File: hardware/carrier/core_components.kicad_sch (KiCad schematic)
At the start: 52 parts, among them J1 PANEL, J2 CARDKB, J3 HAPTIC, J4 EXT_LED, J5 PIEZ, J8 FRONTLIGHT, M1 Walter, Q1 UMH3N, Q2 SI1308EDL, Q3 MMST3904, SW1 KMR221GLFS, U1 CP2102N-A02-GQFN24, U2 SN74LVC2G126DCUR, U3 DRV2605LDGSR, U4 LIS2DW12TR

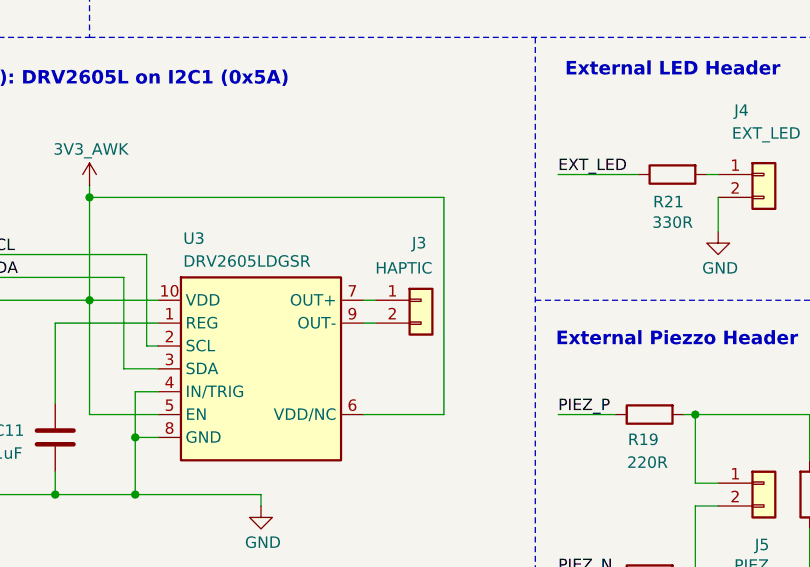
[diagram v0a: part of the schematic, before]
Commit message: Hand routed the carrier board
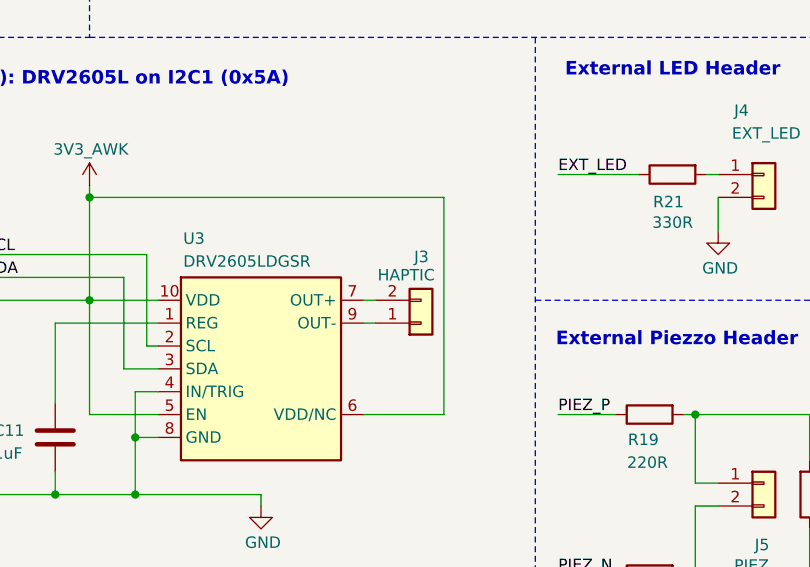
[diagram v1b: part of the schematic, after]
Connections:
- net at J3.1 (Pin_1): now also U3.9 (OUT-); no longer U3.7 (OUT+)
- net at J3.2 (Pin_2): now also U3.7 (OUT+); no longer U3.9 (OUT-)
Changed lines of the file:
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@@
 	(wire
 		(pts
+			(xy 351.79 162.56) (xy 353.06 162.56)
+		)
+		(stroke
+			(width 0)
+			(type default)
+		)
+	)
+	(wire
+		(pts
 			(xy 184.15 243.84) (xy 195.58 243.84)
 		)
@@
 	(wire
 		(pts
-			(xy 351.79 160.02) (xy 353.06 160.02)
-		)
-		(stroke
-			(width 0)
-			(type default)
-		)
-	)
-	(wire
-		(pts
 			(xy 87.63 198.12) (xy 92.71 198.12)
 		)
@@
 	(wire
 		(pts
-			(xy 351.79 162.56) (xy 353.06 162.56)
+			(xy 255.27 203.2) (xy 255.27 207.01)
 		)
 		(stroke
@@
 	(wire
 		(pts
-			(xy 255.27 203.2) (xy 255.27 207.01)
+			(xy 25.4 240.03) (xy 25.4 236.22)
 		)
 		(stroke
@@
 	(wire
 		(pts
-			(xy 25.4 240.03) (xy 25.4 236.22)
+			(xy 401.32 172.72) (xy 388.62 172.72)
 		)
 		(stroke
@@
 	(wire
 		(pts
-			(xy 401.32 172.72) (xy 388.62 172.72)
+			(xy 351.79 160.02) (xy 353.06 160.02)
 		)
 		(stroke
@@
 	(symbol
 		(lib_id "Connector_Generic:Conn_01x02")
-		(at 358.14 160.02 0)
+		(at 358.14 162.56 0)
+		(mirror x)
 		(unit 1)
 		(body_style 1)
@@
 		(dnp no)
 		(property "Reference" "J3"
-			(at 357.124 153.67 0)
+			(at 357.378 155.194 0)
 			(show_name no)
 			(do_not_autoplace no)
@@
 		)
 		(property "Value" "HAPTIC"
-			(at 353.06 156.464 0)
+			(at 359.664 157.226 0)
 			(show_name no)
 			(do_not_autoplace no)
@@
 					(size 1.27 1.27)
 				)
-				(justify left)
+				(justify right)
 			)
 		)
 		(property "Footprint" "Connector_JST:JST_SH_SM02B-SRSS-TB_1x02-1MP_P1.00mm_Horizontal"
-			(at 354.33 163.83 0)
+			(at 354.33 158.75 0)
 			(hide yes)
 			(show_name no)
@@
 		)
 		(property "Datasheet" "~"
-			(at 354.33 166.37 0)
+			(at 354.33 156.21 0)
 			(hide yes)
 			(show_name no)
@@
 		)
 		(property "Description" "Generic connector, single row, 01x02, script generated (kicad-library-utils/schlib/autogen/connector/)"
-			(at 354.33 168.91 0)
+			(at 354.33 153.67 0)
 			(hide yes)
 			(show_name no)
@@
 		)
 		(property "MPN" "SM02B-SRSS-TB"
-			(at 358.14 175.26 0)
+			(at 358.14 147.32 0)
 			(hide yes)
 			(show_name no)
@@
 		)
 		(property "LCSC" "C160402"
-			(at 358.14 177.8 0)
+			(at 358.14 144.78 0)
 			(hide yes)
 			(show_name no)
@@
 		)
 		(property "DNP" "DNP"
-			(at 358.14 180.34 0)
+			(at 358.14 142.24 0)
 			(hide yes)
 			(show_name no)
@@
 			"7b9a8882-aa2e-431e-bf01-451e054ae998" "80c49014-8df1-45e0-bfb6-6b63e6c333c9"
 			"84fcbab0-daa1-441c-874c-d63bd37a6251" "893e9b16-a7fc-43d8-853a-b314d8663c14"
-			"98fd6db6-d9ea-458d-8c49-e6b2d6b83486" "9bb44a5b-619a-4aaf-8cb0-35d2e10df53e"
+			"8c233fb2-0ba5-4eea-abec-9d8ffd5e9732" "98fd6db6-d9ea-458d-8c49-e6b2d6b83486"
 			"9f22073a-410c-4aee-a30b-ad5186729213" "a0da2b73-a2a1-4d24-9a9f-cf38ae3a1fd7"
 			"a953f703-3acc-4787-b26e-e90b6145f523" "b0278a24-2b33-4994-bc8c-72e411dc1c9f"
@@
 			"bffd956c-f161-48de-985b-f6187bbc6fd6" "c4799d51-3879-49ad-8428-ed96becc74f0"
 			"d2f5092c-1419-4f51-8214-861f91826950" "d3b6f78e-d011-463f-a13e-16578a490a0d"
-			"db67fcb9-54b2-4177-b047-ff10635e9f6d" "e7c002b9-f0a2-422c-8b31-199ba72e29b9"
+			"de0bbf4a-c8a4-40cf-b604-08bc230e503a" "e7c002b9-f0a2-422c-8b31-199ba72e29b9"
 			"e7f922ab-438b-4da8-8d8e-1e1073d0e6ed" "ead65bd9-2815-4738-b9c9-cfb123010ba6"
 			"eb069365-4d9c-44dd-b591-d3c1ad9e9259" "ee4224c8-18f3-4603-b81d-e0db50f4dac2"
